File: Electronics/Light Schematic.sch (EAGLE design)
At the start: 12 parts, among them IC1 7805T, U1 328P

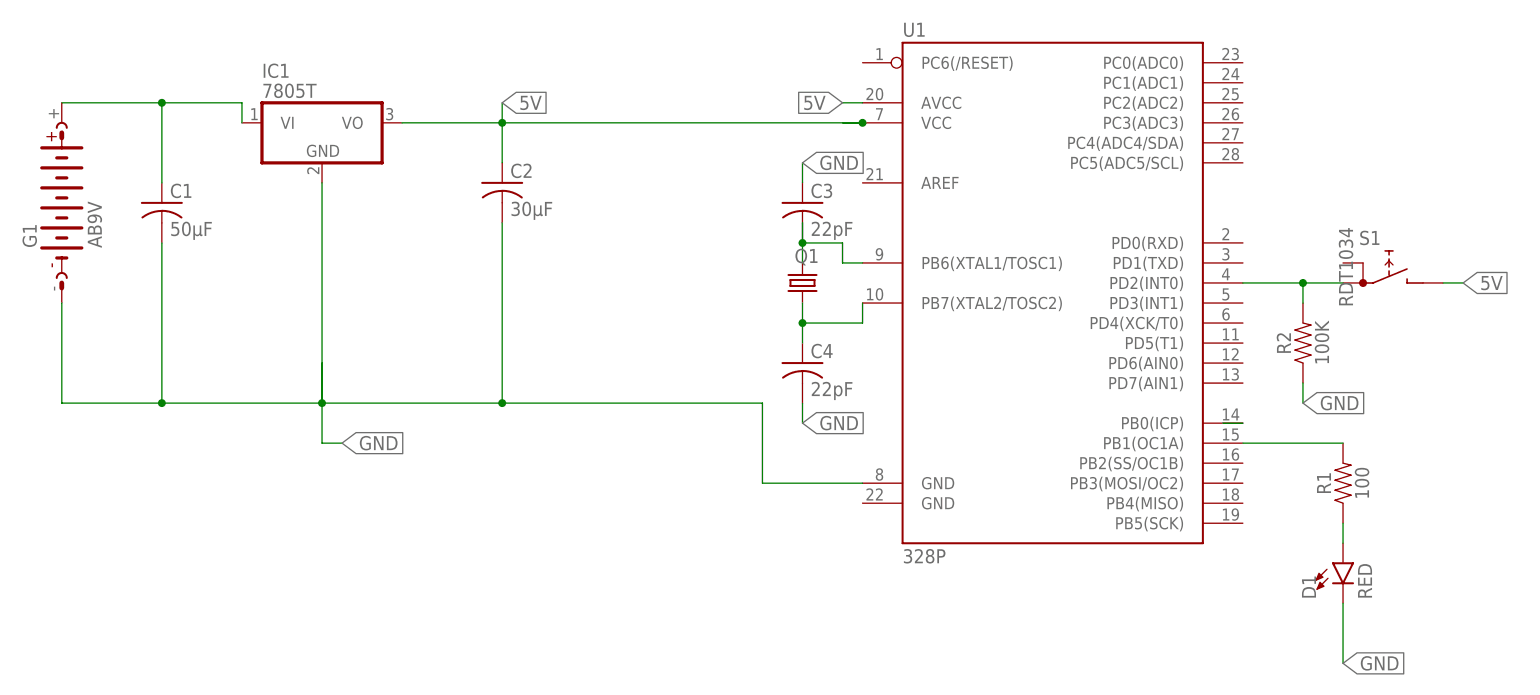
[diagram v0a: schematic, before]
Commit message: updated light box schematic and PCB
- connected pin 8 and pin 22
- changed the battery to header pins
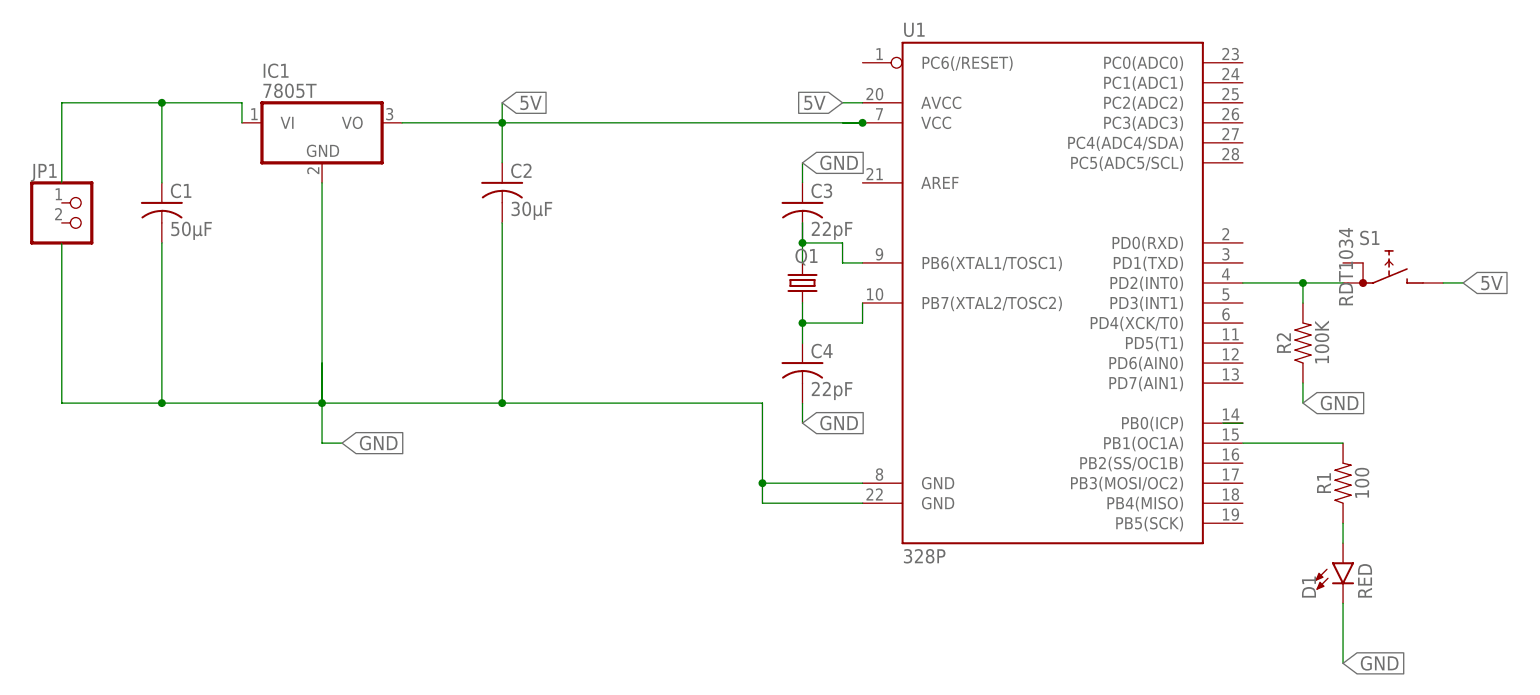
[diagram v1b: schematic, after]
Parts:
- removed G1: AB9V, battery:AB9V
- added JP1: (no value), pinhead:PINHD-1X2
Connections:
- net GND: now also U1.GND@2; no longer G1.-
- net N$1: no longer G1.+
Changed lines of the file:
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@@
 </classes>
 <parts>
-<part name="G1" library="battery" library_urn="urn:adsk.eagle:library:109" deviceset="AB9V" device="" package3d_urn="urn:adsk.eagle:package:4600/1"/>
 <part name="R1" library="SparkFun-Resistors" library_urn="urn:adsk.eagle:library:532" deviceset="100KOHM" device="-0402-1/16W-1%" package3d_urn="urn:adsk.eagle:package:39657/1" value="100"/>
 <part name="IC1" library="linear" library_urn="urn:adsk.eagle:library:262" deviceset="78*" device="T" package3d_urn="urn:adsk.eagle:package:16414/1" technology="05"/>
@@
 <part name="C3" library="adafruit" library_urn="urn:adsk.eagle:library:420" deviceset="C-US" device="C0805" package3d_urn="urn:adsk.eagle:package:6240337/1" value="22pF"/>
 <part name="C4" library="adafruit" library_urn="urn:adsk.eagle:library:420" deviceset="C-US" device="C0805" package3d_urn="urn:adsk.eagle:package:6240337/1" value="22pF"/>
+<part name="JP1" library="pinhead" library_urn="urn:adsk.eagle:library:325" deviceset="PINHD-1X2" device="" package3d_urn="urn:adsk.eagle:package:22435/2"/>
 </parts>
 <sheets>
@@
 </plain>
 <instances>
-<instance part="G1" gate="G$1" x="-33.02" y="91.44" smashed="yes" rot="R90">
-<attribute name="NAME" x="-36.195" y="85.725" size="1.778" layer="95" rot="R90"/>
-<attribute name="VALUE" x="-27.94" y="85.725" size="1.778" layer="96" rot="R90"/>
-</instance>
 <instance part="R1" gate="G$1" x="129.54" y="55.88" smashed="yes" rot="R90">
 <attribute name="NAME" x="128.016" y="55.88" size="1.778" layer="95" font="vector" rot="R90" align="bottom-center"/>
@@
 <attribute name="VALUE" x="61.976" y="66.929" size="1.778" layer="96"/>
 </instance>
+<instance part="JP1" gate="G$1" x="-30.48" y="88.9" smashed="yes">
+<attribute name="NAME" x="-36.83" y="94.615" size="1.778" layer="95"/>
+<attribute name="VALUE" x="-36.83" y="83.82" size="1.778" layer="96"/>
+</instance>
 </instances>
 <busses>
@@
 <net name="N$1" class="0">
 <segment>
-<pinref part="G1" gate="G$1" pin="+"/>
 <pinref part="IC1" gate="A1" pin="VI"/>
 <wire x1="-33.02" y1="104.14" x2="-20.32" y2="104.14" width="0.1524" layer="91"/>
@@
 <pinref part="C1" gate="G$1" pin="1"/>
 <wire x1="-20.32" y1="104.14" x2="-20.32" y2="93.98" width="0.1524" layer="91"/>
+<wire x1="-33.02" y1="104.14" x2="-33.02" y2="93.98" width="0.1524" layer="91"/>
 </segment>
 </net>
@@
 <wire x1="22.86" y1="88.9" x2="22.86" y2="66.04" width="0.1524" layer="91"/>
 <pinref part="C2" gate="G$1" pin="2"/>
-<pinref part="G1" gate="G$1" pin="-"/>
-<wire x1="-33.02" y1="78.74" x2="-33.02" y2="66.04" width="0.1524" layer="91"/>
+<wire x1="-33.02" y1="86.36" x2="-33.02" y2="66.04" width="0.1524" layer="91"/>
 <wire x1="-33.02" y1="66.04" x2="-20.32" y2="66.04" width="0.1524" layer="91"/>
 <junction x="-20.32" y="66.04"/>
@@
 <pinref part="U1" gate="G$1" pin="GND@1"/>
 <wire x1="55.88" y1="55.88" x2="68.58" y2="55.88" width="0.1524" layer="91"/>
+<wire x1="55.88" y1="55.88" x2="55.88" y2="53.34" width="0.1524" layer="91"/>
+<junction x="55.88" y="55.88"/>
+<pinref part="U1" gate="G$1" pin="GND@2"/>
+<wire x1="55.88" y1="53.34" x2="68.58" y2="53.34" width="0.1524" layer="91"/>
 </segment>
 <segment>
